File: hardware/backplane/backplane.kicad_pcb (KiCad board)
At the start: 2 copper layers, 200 x 124 mm, 105 parts, among them J1 C96ABC, J10 Conn_Coaxial_Power, J2 C96ABC, J3 C96ABC, J4 C96ABC, J5 C96ABC, J6 C96ABC, J7 C96ABC, J8 C96ABC, J9 C96ABC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

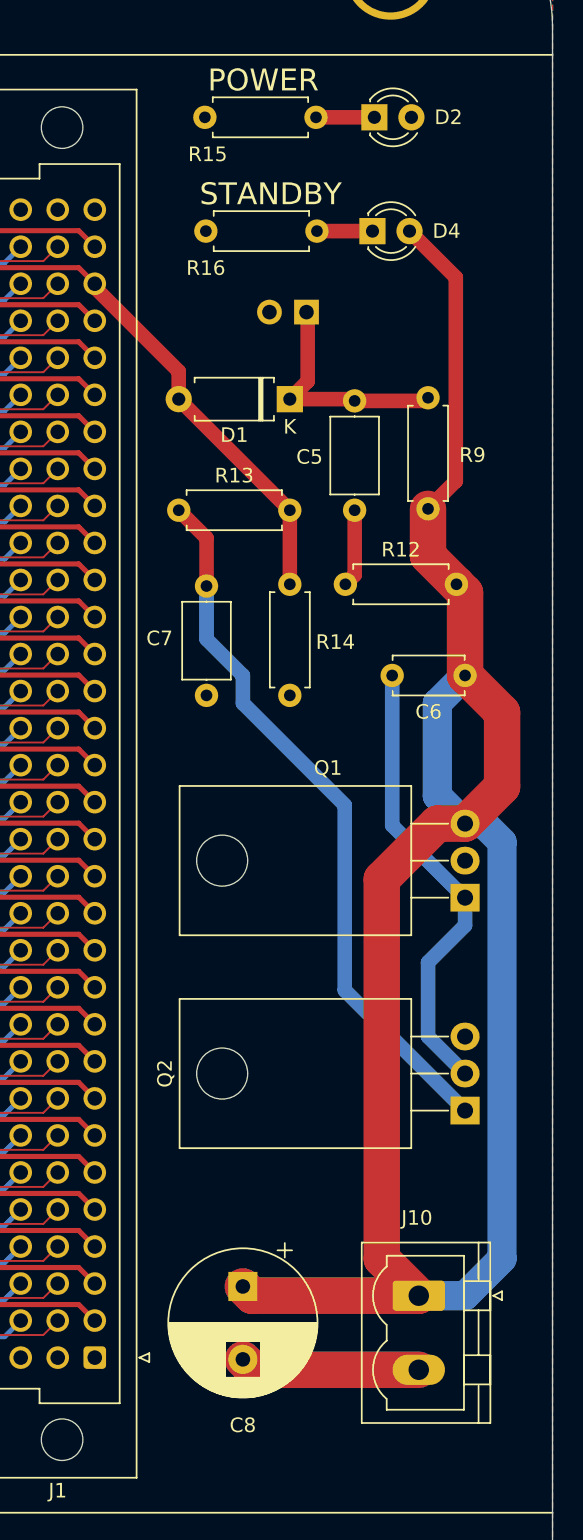
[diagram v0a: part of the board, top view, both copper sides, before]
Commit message: start adding reverse voltage protection
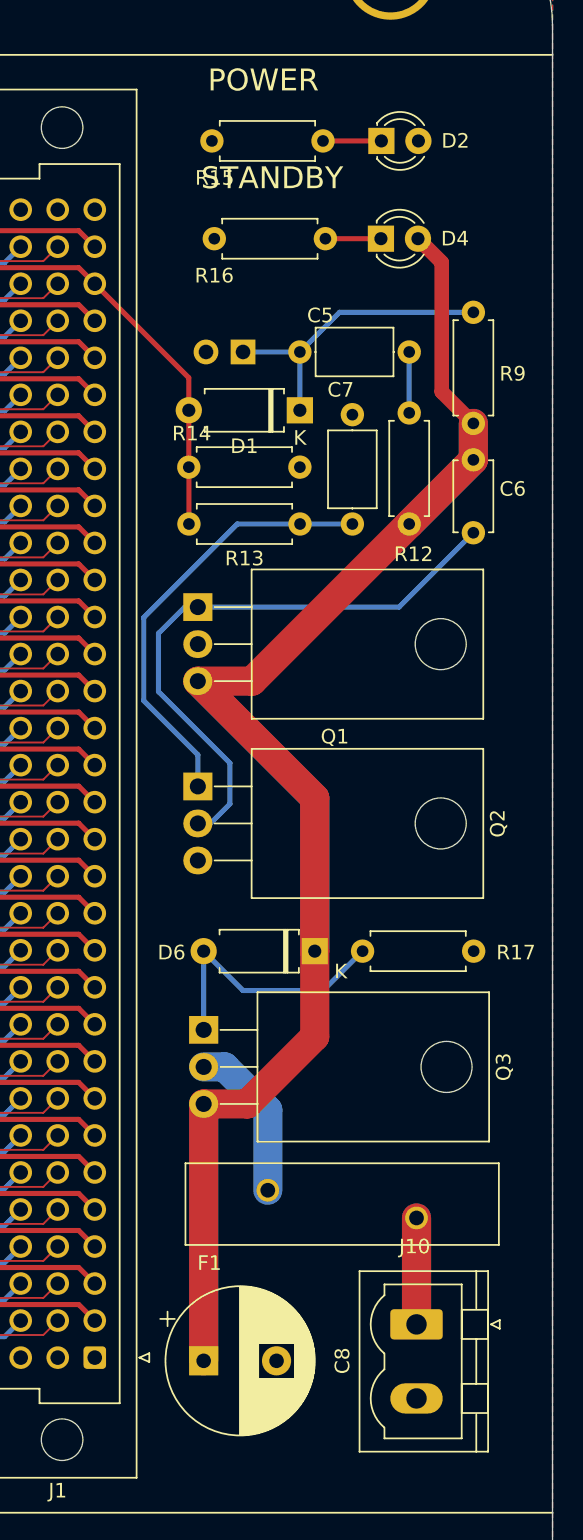
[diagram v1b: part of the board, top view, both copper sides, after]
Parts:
- added D6: D_Zener, Diode_THT:D_A-405_P7.62mm_Horizontal, F.Cu at (227.8, 102.0)
- added F1: Fuse, Fuse:Fuse_BelFuse_0ZRE0125FF_L21.2mm_W5.3mm, F.Cu at (224.6, 118.4)
- added Q3: FQP27P06, Package_TO_SOT_THT:TO-220-3_Horizontal_TabDown, F.Cu at (220.2, 107.4)
- added R17: 100, Resistor_THT:R_Axial_DIN0207_L6.3mm_D2.5mm_P7.62mm_Horizontal, F.Cu at (238.7, 102.0)
- moved Q2 28.8 mm to (219.8, 90.7), turned to 270 degrees
- moved Q1 27.1 mm to (219.8, 78.4), turned to 270 degrees
- moved C7 21.7 mm to (230.3, 65.2), turned to 270 degrees
- moved C6 14.8 mm to (238.7, 68.3), turned to 270 degrees
- moved R12 12.5 mm to (234.2, 65.1), turned to 270 degrees
- moved C5 11.5 mm to (234.2, 60.9), turned to 180 degrees
- moved R14 10.6 mm to (219.1, 68.8), turned to 0 degrees
- moved R13 8.37 mm to (226.8, 72.7), turned to 180 degrees
- moved R9 6.63 mm to (238.7, 58.2)
- moved C8 5.77 mm to (220.2, 130.1), turned to 0 degrees
- moved SW5 5.14 mm to (222.8, 60.9)
- moved J10 1.97 mm to (234.8, 127.6)
- moved D2 1.69 mm to (232.3, 46.4)
- moved R15 1.69 mm to (220.7, 46.4)
- moved D1 1.03 mm to (226.8, 64.9)
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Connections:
- J10 pad 1: +5V -> Net-(F1-Pad2)
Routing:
- net +5V: track 170.1 -> 145.0 mm, vias 0 -> 1
- net GND: track 90.7 -> 66.0 mm
- net Net-(C7-Pad2): track 49.3 -> 30.1 mm
- net Net-(D6-Pad2): track 0.00 -> 18.5 mm
- net Net-(F1-Pad2): track 0.00 -> 14.6 mm
- net +VDC: track 0.00 -> 11.1 mm
- net Net-(C6-Pad2): track 31.5 -> 40.9 mm
- net A30: track 170.6 -> 163.9 mm
- net Net-(C5-Pad2): track 16.1 -> 20.9 mm
- net Net-(C5-Pad1): track 5.34 -> 4.18 mm
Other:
- net class Power removed
- net class power added: clearance 0.15, trace_width 0.35, via_dia 0.8, via_drill 0.4
- net class rails added: clearance 0.2, trace_width 2, via_dia 0.8, via_drill 0.4

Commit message: backplane: fix some values and footprints
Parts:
- R17: value 100 -> 100k

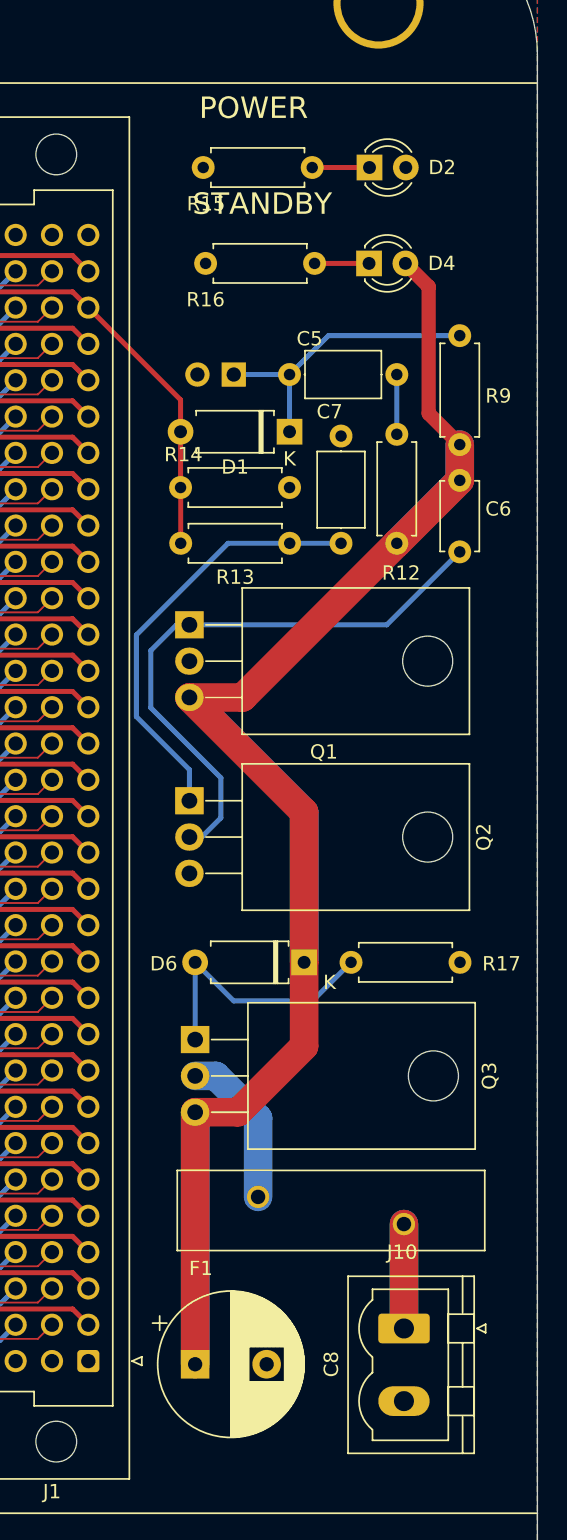
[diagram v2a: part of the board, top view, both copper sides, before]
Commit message: backplane: remove fuse
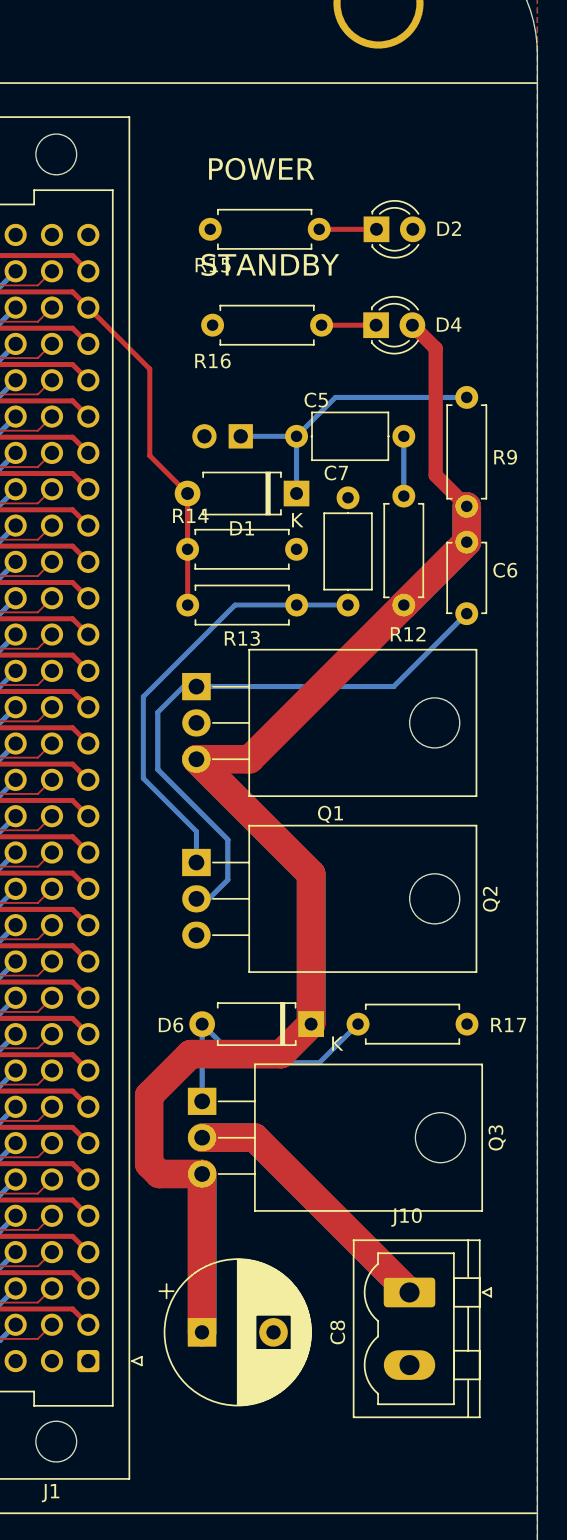
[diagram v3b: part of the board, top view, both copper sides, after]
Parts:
- removed F1: Fuse, Fuse:Fuse_BelFuse_0ZRE0125FF_L21.2mm_W5.3mm
- D6: value D_Zener -> 4.3V
- R17: value 100k -> 100
- moved R12 4.35 mm to (234.7, 69.4)
- moved R14 4.35 mm to (219.6, 73.1)
- moved C6 4.35 mm to (239.1, 72.6)
- moved C5 4.35 mm to (234.7, 65.2)
- moved D2 4.35 mm to (232.8, 50.7)
- moved D4 4.35 mm to (232.8, 57.5)
- moved R15 4.35 mm to (221.2, 50.7)
- moved R16 4.35 mm to (221.4, 57.5)
- moved SW5 4.35 mm to (223.3, 65.2)
- moved R9 4.35 mm to (239.1, 62.5)
- moved C7 4.35 mm to (230.8, 69.5)
- moved D1 4.35 mm to (227.2, 69.2)
- moved Q1 4.35 mm to (220.2, 82.7)
- moved Q2 4.35 mm to (220.2, 95.0)
- moved R13 4.35 mm to (227.2, 77.0)
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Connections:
- J10 pad 1: Net-(F1-Pad2) -> +VDC
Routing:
- net +VDC: track 11.1 -> 38.0 mm
- net Net-(F1-Pad2): track 14.6 -> 0.00 mm
- net +5V: track 145.0 -> 138.7 mm
- net A30: track 163.9 -> 168.4 mm
